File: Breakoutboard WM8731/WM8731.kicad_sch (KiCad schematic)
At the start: 42 parts

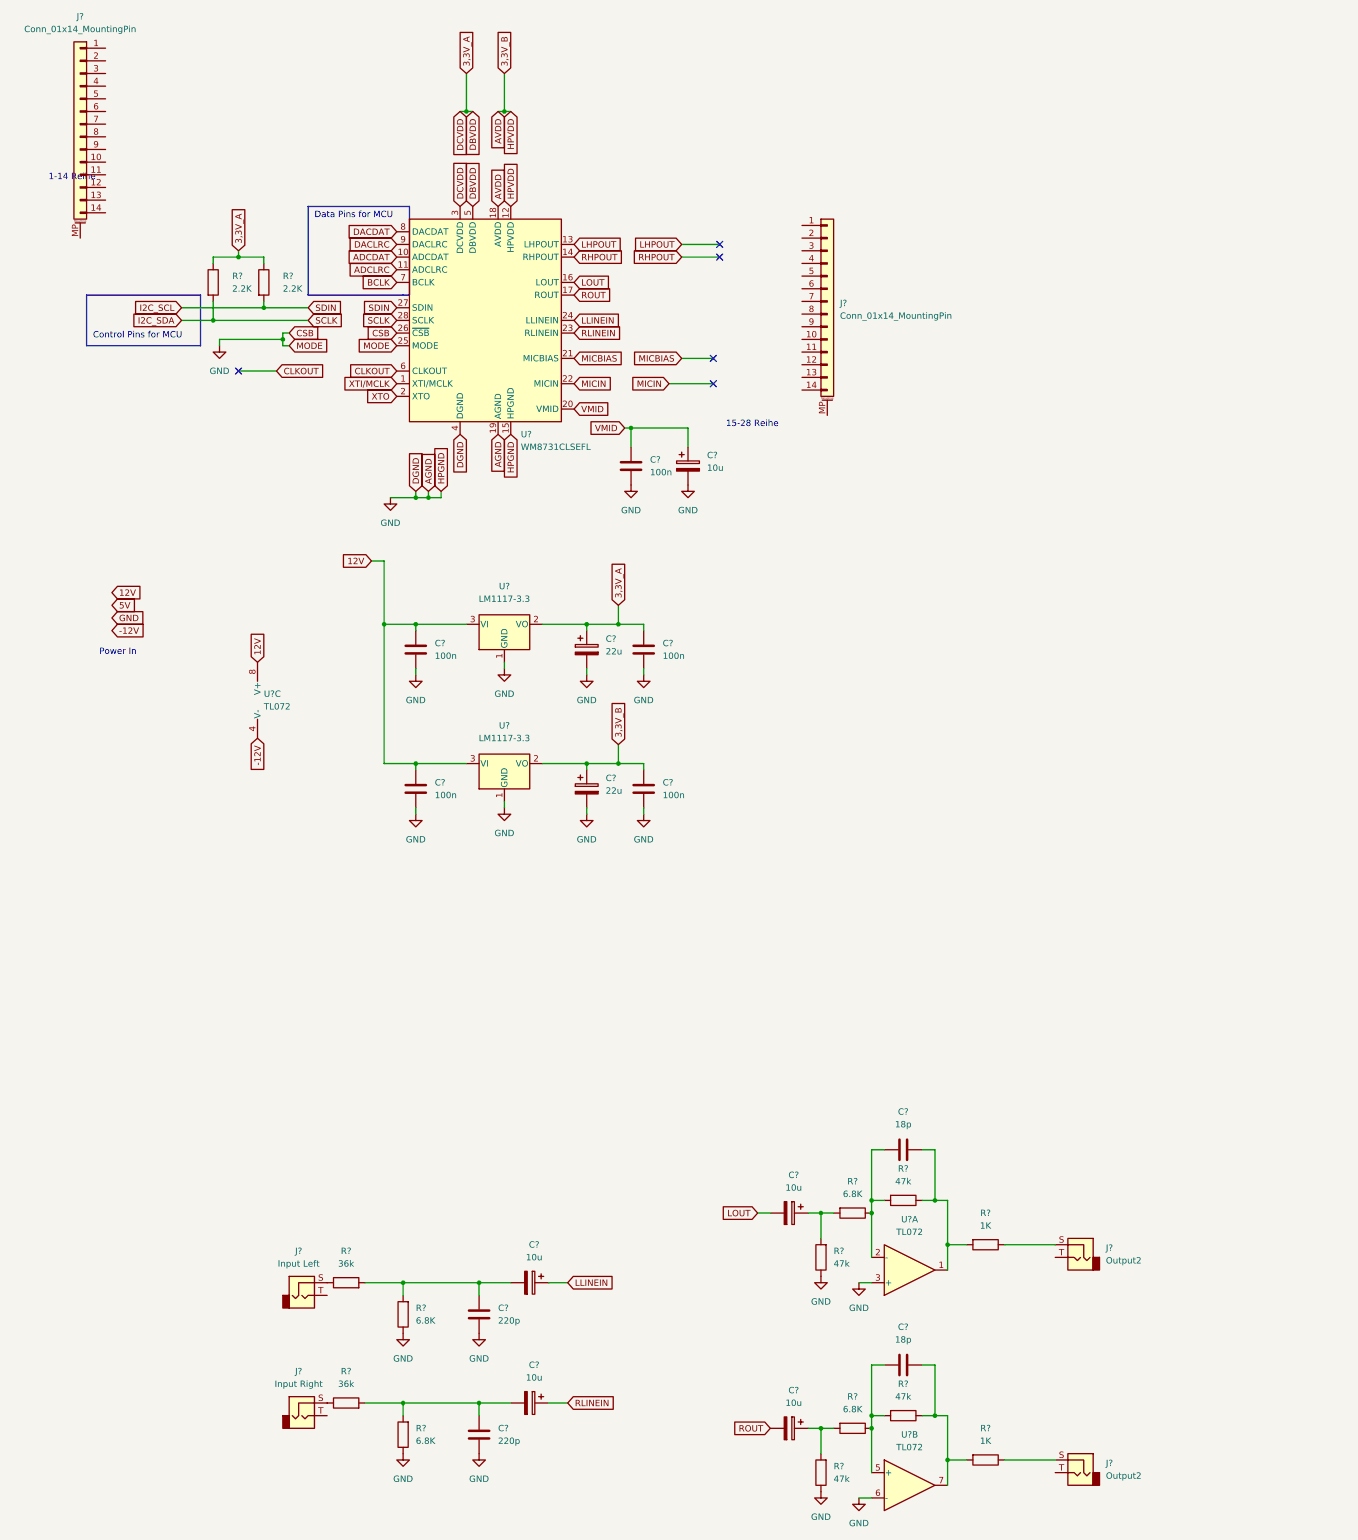
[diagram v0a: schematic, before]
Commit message: Changed WM8731 breakout board structure and header pins
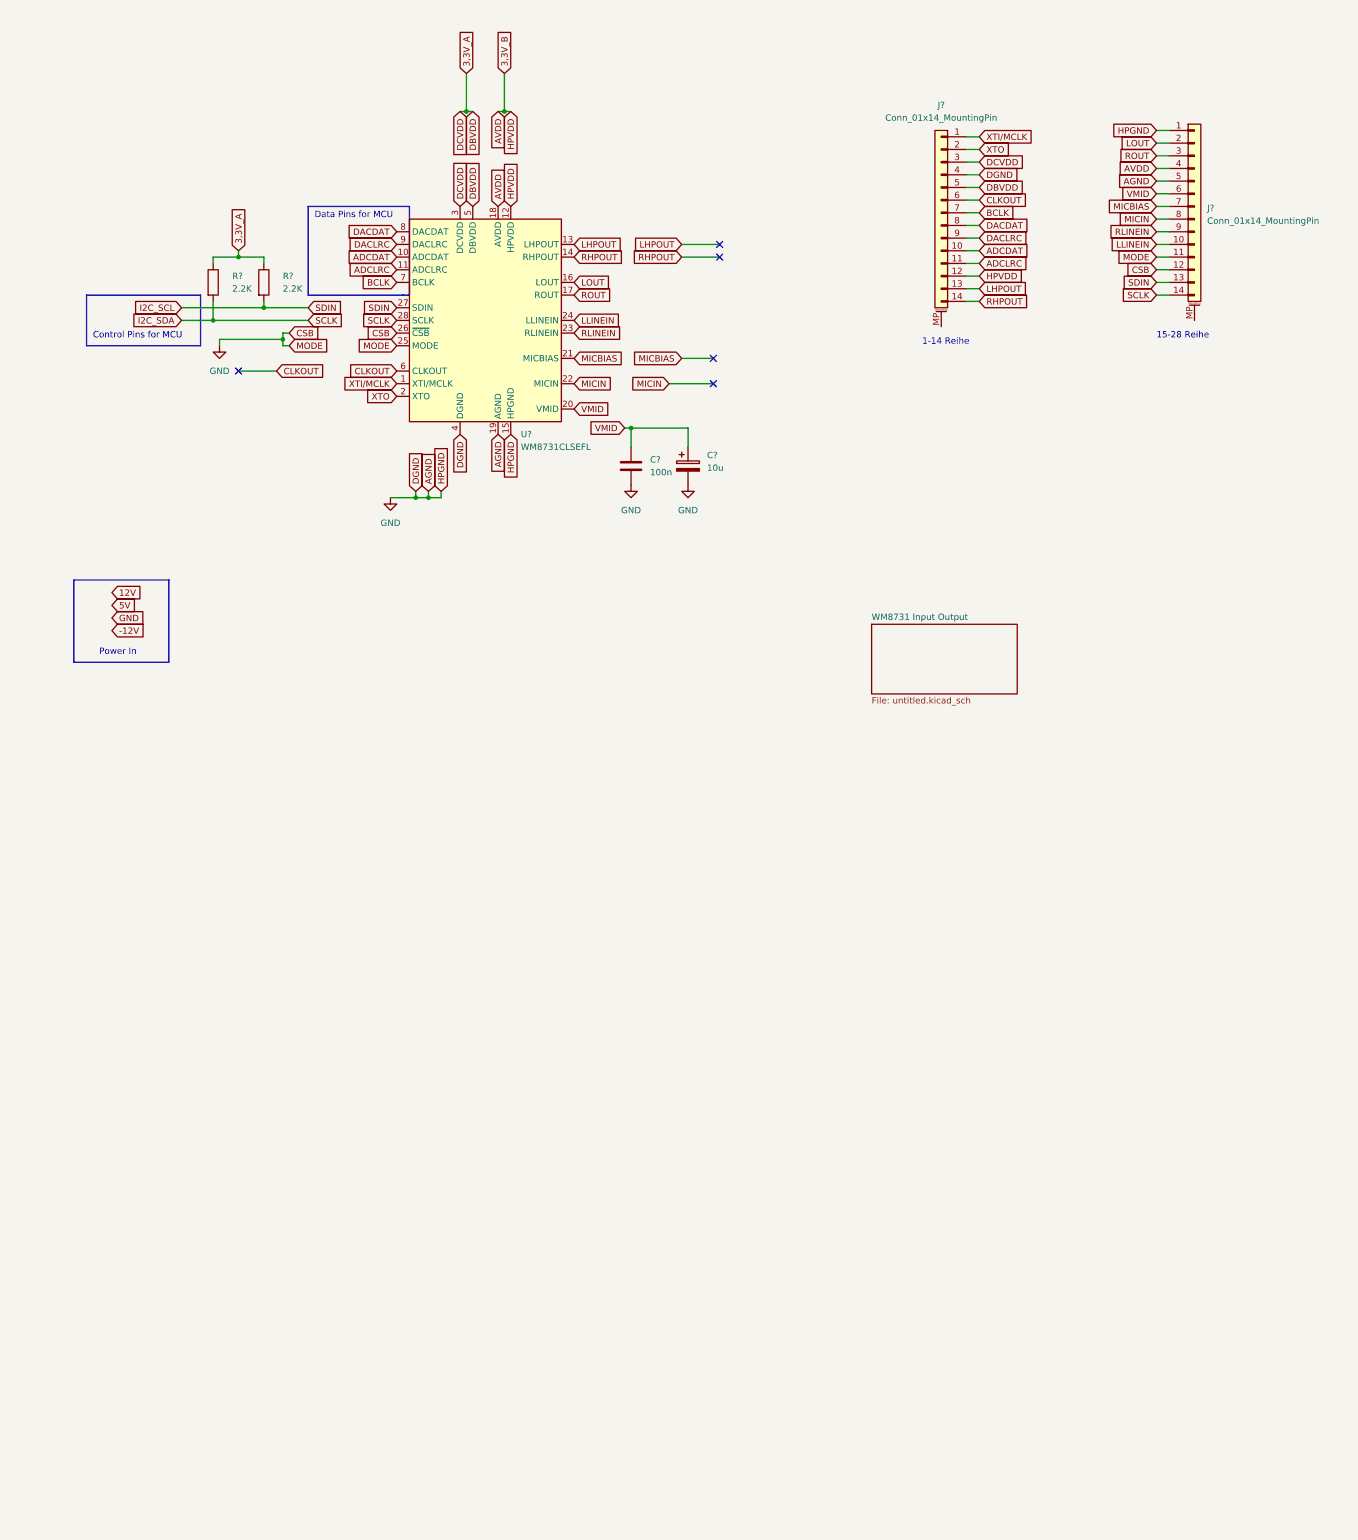
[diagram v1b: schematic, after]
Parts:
- removed C? (x2): 220p, symbol Device:C
- removed C? (x2): 22u, symbol Device:C_Polarized
- removed C? (x4): 10u, symbol Device:C_Polarized
- removed C? (x4): 100n, symbol Device:C
- removed C? (x2): 18p, symbol Device:C
- removed J? (x2): Output2, symbol Connector:AudioJack2
- removed J?: Input Left, symbol Connector:AudioJack2
- removed J?: Input Right, symbol Connector:AudioJack2
- removed R? (x4): 6.8K, symbol Device:R
- removed R? (x4): 47k, symbol Device:R
- removed R? (x2): 36k, symbol Device:R
- removed R? (x2): 1K, symbol Device:R
- removed U? (x2): LM1117-3.3, symbol Regulator_Linear:LM1117-3.3
- removed U? (x3): TL072, symbol Amplifier_Operational:TL072
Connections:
- net 3,3V_A: now also J?.3 (Pin_3), J?.5 (Pin_5)
- net 3,3V_B: now also J?.12 (Pin_12), J?.4 (Pin_4)
- net ADCDAT: now also J?.10 (Pin_10)
- net ADCLRC: now also J?.11 (Pin_11)
- net BCLK: now also J?.7 (Pin_7)
- net CLKOUT: now also J?.6 (Pin_6)
- net DACDAT: now also J?.8 (Pin_8)
- net DACLRC: now also J?.9 (Pin_9)
- net GND: now also J?.1 (Pin_1), J?.11 (Pin_11), J?.12 (Pin_12), J?.4 (Pin_4), J?.5 (Pin_5)
- net I2C_SCL: now also J?.13 (Pin_13)
- net I2C_SDA: now also J?.14 (Pin_14)
- net LHPOUT: now also J?.13 (Pin_13)
- net LLINEIN: now also J?.10 (Pin_10)
- net LOUT: now also J?.2 (Pin_2)
- net MICBIAS: now also J?.7 (Pin_7)
- net MICIN: now also J?.8 (Pin_8)
- net RHPOUT: now also J?.14 (Pin_14)
- net RLINEIN: now also J?.9 (Pin_9)
- net ROUT: now also J?.3 (Pin_3)
- net VMID: now also J?.6 (Pin_6)
- net XTI/MCLK: now also J?.1 (Pin_1)
- net XTO: now also J?.2 (Pin_2)
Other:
- added sheet WM8731 Input Output (untitled.kicad_sch)
- moved on the sheet: J?

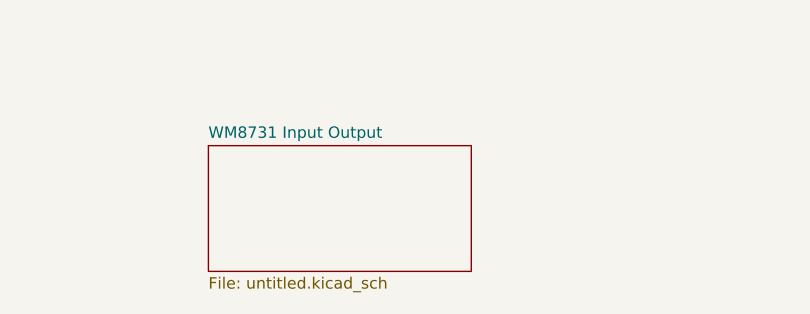
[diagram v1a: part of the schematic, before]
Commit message: renamed untitled -> WM8731 Input Output
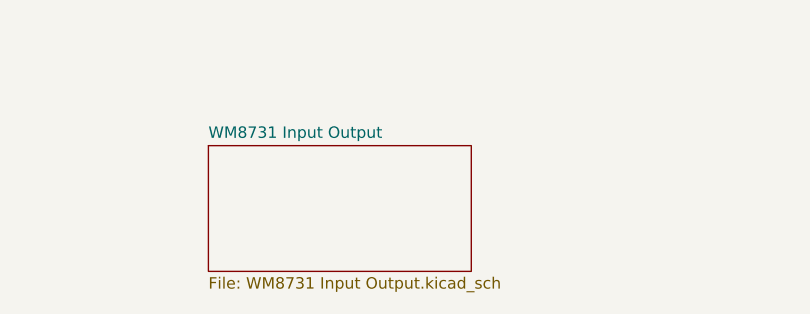
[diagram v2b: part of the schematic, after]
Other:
- sheet WM8731 Input Output: file untitled.kicad_sch -> WM8731 Input Output.kicad_sch
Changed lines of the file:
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@@
       (effects (font (size 1.27 1.27)) (justify left bottom))
     )
-    (property "Sheet file" "untitled.kicad_sch" (id 1) (at 181.61 155.5246 0)
+    (property "Sheet file" "WM8731 Input Output.kicad_sch" (id 1) (at 181.61 155.5246 0)
       (effects (font (size 1.27 1.27)) (justify left top))
     )

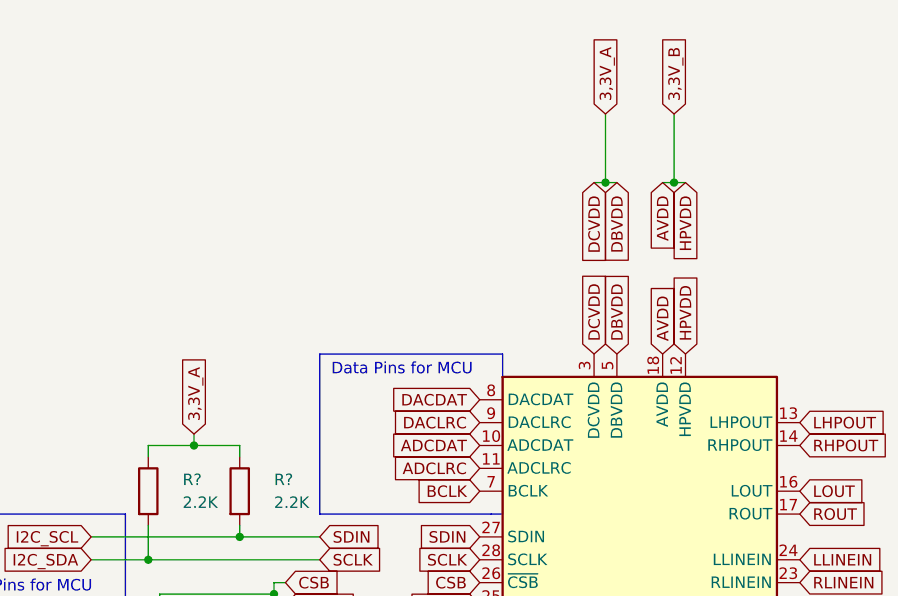
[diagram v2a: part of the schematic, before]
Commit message: reworked power symbols and ESP32 schematic
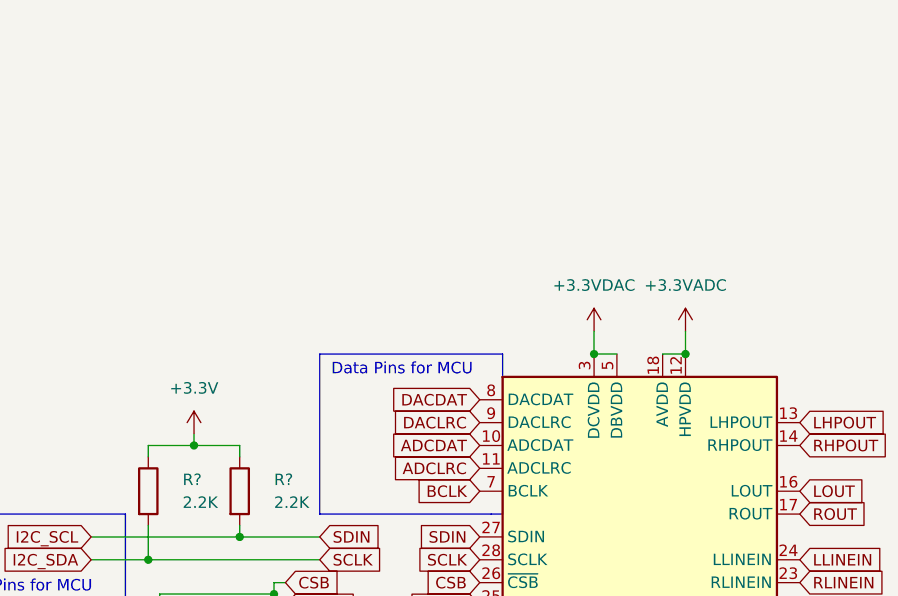
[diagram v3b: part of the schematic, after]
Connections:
- removed net 3,3V_A: J?.3 (Pin_3), J?.5 (Pin_5), R?.1, R?.1, U?.3 (DCVDD), U?.5 (DBVDD)
- net 3,3V_B renamed +3.3VADC
- net +3.3VADC: no longer J?.12 (Pin_12), J?.4 (Pin_4)
- new net +3.3VDAC: U?.3 (DCVDD), U?.5 (DBVDD)
- new net +3V3: R?.1, R?.1
- new net AVDD: J?.4 (Pin_4)
- new net DBVDD: J?.5 (Pin_5)
- new net DCVDD: J?.3 (Pin_3)
- new net HPVDD: J?.12 (Pin_12)
